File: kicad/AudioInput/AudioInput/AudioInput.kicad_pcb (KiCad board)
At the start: 2 copper layers, 43.2 x 48.3 mm, 52 parts, among them J1 EXPAN2, J2 EXPAN1, K1 G6K-2, Q1 BS250, Q2 2N7000, U1 MCP4651, U2 LM324, U3 CD4052B

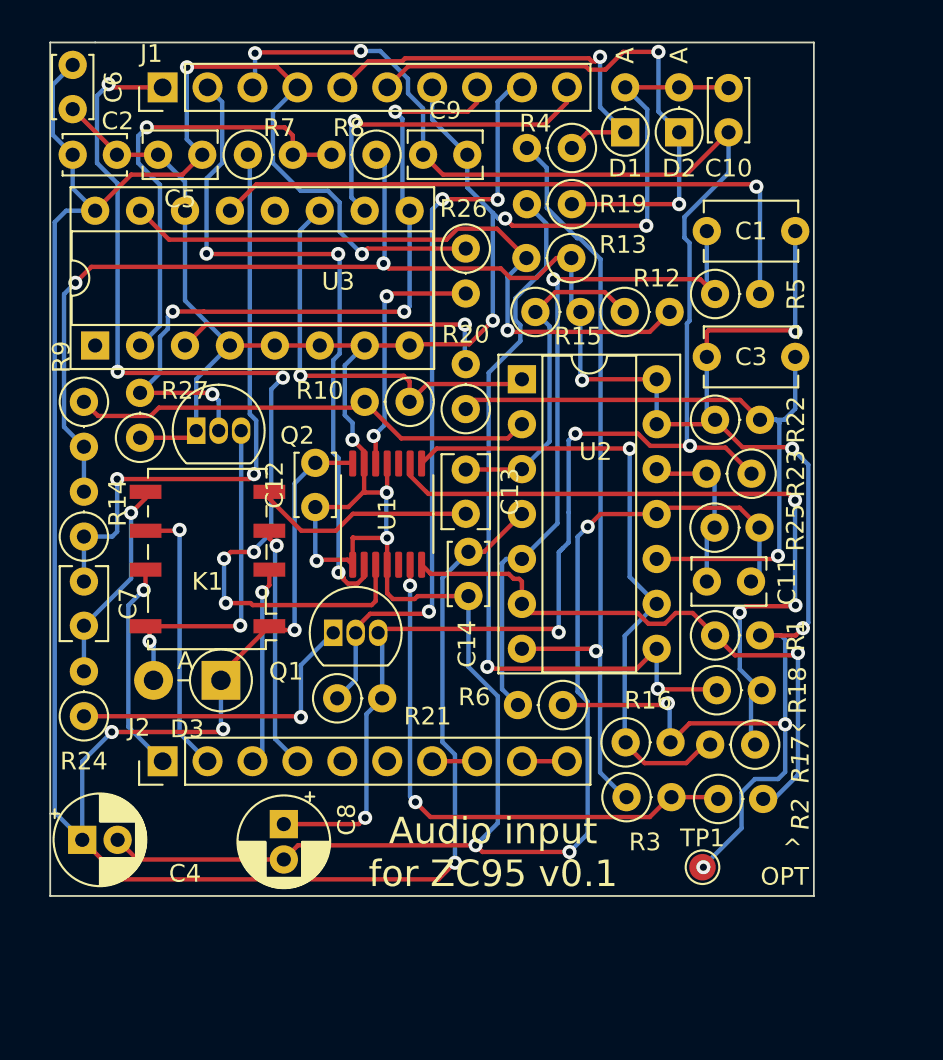
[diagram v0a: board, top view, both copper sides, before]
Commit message: audio input with basic threshold pattern working
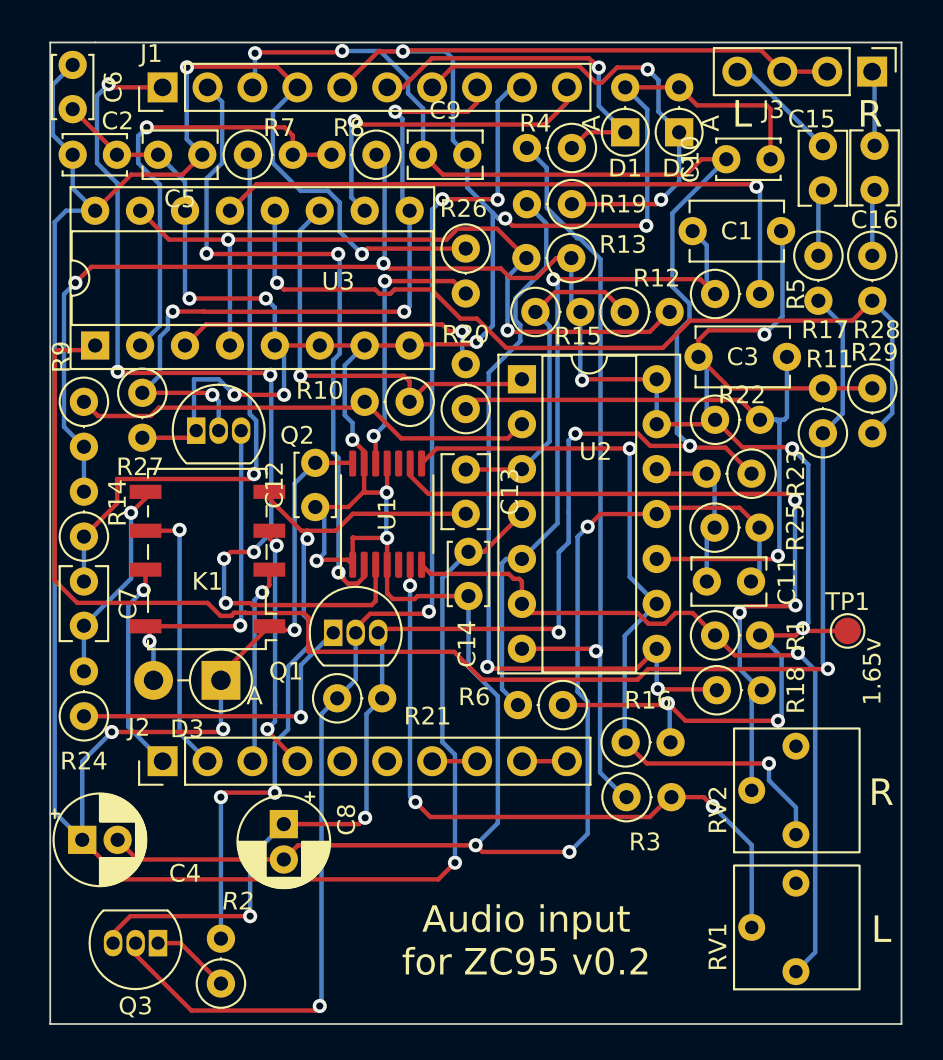
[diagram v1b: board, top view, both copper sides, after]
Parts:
- added C15: 1uF, Capacitor_THT:C_Rect_L4.0mm_W2.5mm_P2.50mm, F.Cu at (173.2, 69.4)
- added C16: 1uF, Capacitor_THT:C_Rect_L4.0mm_W2.5mm_P2.50mm, F.Cu at (176.1, 69.3)
- added J3: INT INPUT, Connector_PinHeader_2.54mm:PinHeader_1x04_P2.54mm_Vertical, F.Cu at (176.0, 65.2)
- added Q3: BS250, Package_TO_SOT_THT:TO-92_Inline, F.Cu at (135.6, 114.4)
- added R11: 150k, Resistor_THT:R_Axial_DIN0207_L6.3mm_D2.5mm_P2.54mm_Vertical, F.Cu at (173.2, 85.6)
- added R28: 100k, Resistor_THT:R_Axial_DIN0207_L6.3mm_D2.5mm_P2.54mm_Vertical, F.Cu at (176.0, 75.6)
- added R29: 150k, Resistor_THT:R_Axial_DIN0207_L6.3mm_D2.5mm_P2.54mm_Vertical, F.Cu at (176.0, 83.1)
- added RV1: 50k, Library:3362P-1-503, F.Cu at (171.7, 113.5)
- added RV2: 50k, Library:3362P-1-503, F.Cu at (171.7, 105.8)
- R1, R16: value 10k -> 4k7
- R17: value 4k7 -> 100k
- R2: value 4k7 -> 2k7
- moved R2 30.0 mm to (139.2, 116.7), turned to 90 degrees
- moved R17 27.9 mm to (173.0, 75.6), turned to -90 degrees
- moved TP1 15.7 mm to (174.6, 96.8)
- moved R27 2.54 mm to (134.7, 83.3), turned to -90 degrees
- moved C10 1.53 mm to (167.8, 70.1), turned to 0 degrees
- moved C1 0.80 mm to (165.9, 74.2)
- moved C3 0.47 mm to (171.2, 81.3)
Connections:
- J1 pad 5: ADC1 -> GND
- J1 pad 6: ADC2 -> ADC1
- J1 pad 7: GND -> ADC2
- R17 pad 1: Net-(R17-Pad1) -> Net-(C15-Pad2)
- R17 pad 2: Net-(R16-Pad1) -> INT_INPUT_L
- R18 pad 2: Net-(R17-Pad1) -> Net-(R18-Pad2)
- R2 pad 1: Net-(R2-Pad1) -> Net-(Q3-Pad1)
- R2 pad 2: Net-(R1-Pad1) -> Net-(C13-Pad2)
- R27 pad 1: GND -> AUDIO_EN
- R27 pad 2: AUDIO_EN -> GND
- R3 pad 2: Net-(R2-Pad1) -> Net-(R3-Pad2)
- U1 pad 6: Net-(R2-Pad1) -> Net-(R3-Pad2)
- U1 pad 9: Net-(R17-Pad1) -> Net-(R18-Pad2)
- U3 pad 1: unconnected-(U3-Pad1) -> INT_INPUT_L
- U3 pad 12: unconnected-(U3-Pad12) -> INT_INPUT_R
- U3 pad 4: GND -> Net-(R12-Pad2)
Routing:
- net INT_INPUT_L: track 0.00 -> 84.9 mm, vias 0 -> 1
- net INT_INPUT_R: track 0.00 -> 49.0 mm, vias 0 -> 1
- net GND: track 190.1 -> 236.1 mm, vias 10 -> 15
- net Net-(R18-Pad2): track 0.00 -> 43.7 mm, vias 0 -> 3
- net Net-(R17-Pad1): track 40.4 -> 0.00 mm, vias 3 -> 0
- net Net-(R3-Pad2): track 0.00 -> 39.1 mm, vias 0 -> 3
- net Net-(R2-Pad1): track 31.3 -> 0.00 mm, vias 2 -> 0
- net MIC_PWR_DIS: track 42.9 -> 73.2 mm, vias 3 -> 4
- net Net-(C13-Pad2): track 12.6 -> 39.6 mm, vias 0 -> 3
- net 3v3: track 102.4 -> 115.7 mm, vias 6 -> 7
- net Net-(R1-Pad1): track 34.3 -> 43.6 mm
- net Net-(R16-Pad1): track 35.7 -> 43.4 mm, vias 1 -> 2
- net Net-(C15-Pad1): track 0.00 -> 6.58 mm
- net Net-(R12-Pad2): track 37.7 -> 43.7 mm, vias 1 -> 2
- net Net-(Q3-Pad1): track 0.00 -> 4.50 mm
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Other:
- board size 43.2 x 48.3 mm -> 48.1 x 55.5 mm
- board text added: "1.65v"
- board text added: "Audio input for ZC95 v0.2"
- board text added: "L"
- board text added: "R"
- board text removed: "Audio input for ZC95 v0.1"
- board text removed: "^"
- board text removed: "^ OPT"

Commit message: mostly documentation of audio input board
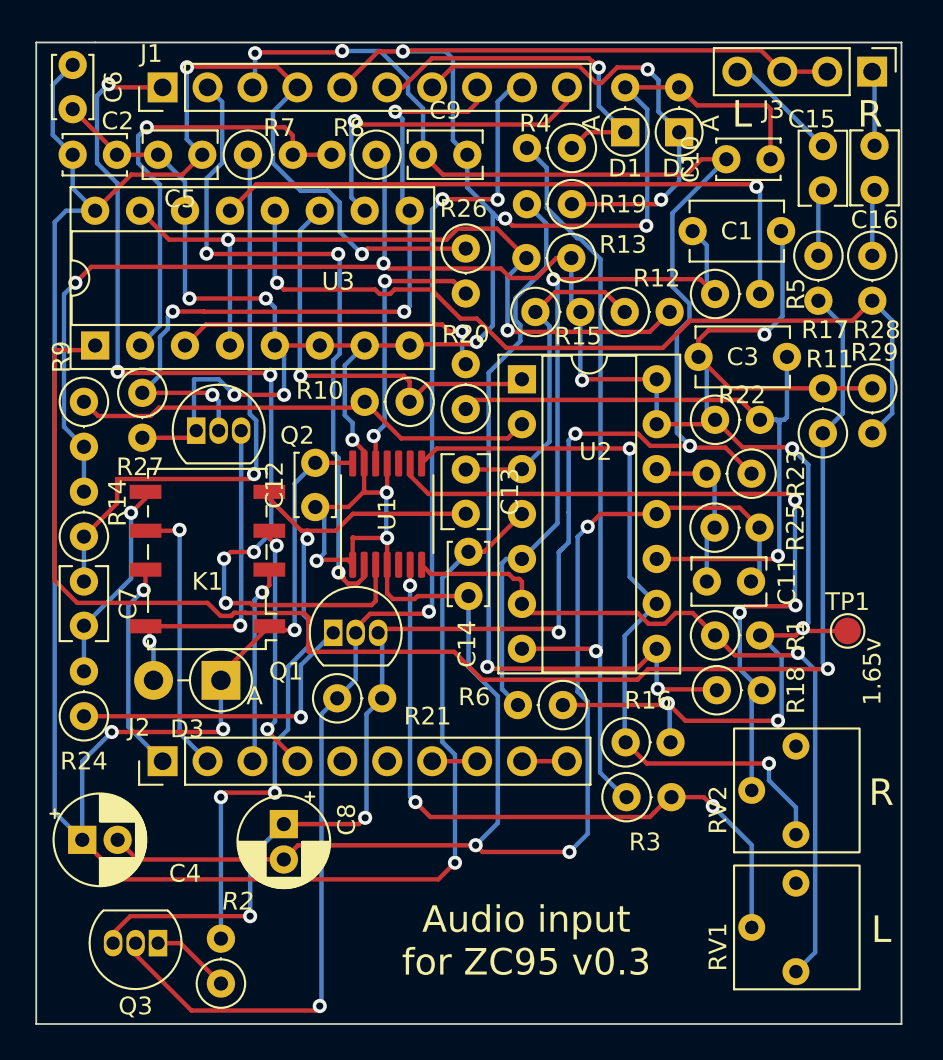
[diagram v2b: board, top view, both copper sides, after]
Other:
- board size 48.1 x 55.5 mm -> 48.9 x 55.5 mm
- board text added: "Audio input for ZC95 v0.3"
- board text removed: "Audio input for ZC95 v0.2"
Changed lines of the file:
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@@
     )
   )
-  (gr_line (start 129.54 63.5) (end 132.08 63.5) (layer "Edge.Cuts") (width 0.1))
+  (gr_line (start 128.75 63.5) (end 132.08 63.5) (layer "Edge.Cuts") (width 0.1))
   (gr_line (start 177.673 63.5) (end 177.673 118.999) (layer "Edge.Cuts") (width 0.1))
-  (gr_line (start 129.54 118.999) (end 129.54 63.5) (layer "Edge.Cuts") (width 0.1))
+  (gr_line (start 128.75 118.999) (end 128.75 63.5) (layer "Edge.Cuts") (width 0.1))
   (gr_line (start 132.08 63.5) (end 177.673 63.5) (layer "Edge.Cuts") (width 0.1))
-  (gr_line (start 177.673 118.999) (end 129.54 118.999) (layer "Edge.Cuts") (width 0.1))
-  (gr_text "Audio input\nfor ZC95 v0.2" (at 156.464 114.3) (layer "F.SilkS")
+  (gr_line (start 177.673 118.999) (end 128.75 118.999) (layer "Edge.Cuts") (width 0.1))
+  (gr_text "Audio input\nfor ZC95 v0.3" (at 156.464 114.3) (layer "F.SilkS")
     (effects (font (size 1.5 1.5) (thickness 0.3)))
   )

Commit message: Audio input board v0.4
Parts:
- removed D1, D2: 3.3v, Diode_THT:D_DO-35_SOD27_P2.54mm_Vertical_AnodeUp
- removed RV1, RV2: 50k, Library:3362P-1-503
- C1: value 3nF -> 3.3nF; footprint Capacitor_THT:C_Disc_D5.1mm_W3.2mm_P5.00mm -> Capacitor_SMD:C_0603_1608Metric_Pad1.08x0.95mm_HandSolder
- C10, C12, C6: footprint Capacitor_THT:C_Disc_D3.4mm_W2.1mm_P2.50mm -> Capacitor_SMD:C_0603_1608Metric_Pad1.08x0.95mm_HandSolder
- C11, C15, C7, C9: footprint Capacitor_THT:C_Rect_L4.0mm_W2.5mm_P2.50mm -> Capacitor_SMD:C_0603_1608Metric_Pad1.08x0.95mm_HandSolder
- C13: value 1uF -> 10uF; footprint Capacitor_THT:C_Rect_L4.0mm_W2.5mm_P2.50mm -> Capacitor_SMD:C_0603_1608Metric_Pad1.08x0.95mm_HandSolder
- C14, C2: value 100nF -> 1uF; footprint Capacitor_THT:C_Disc_D3.4mm_W2.1mm_P2.50mm -> Capacitor_SMD:C_0603_1608Metric_Pad1.08x0.95mm_HandSolder
- C16: value 1uF -> 100nF; footprint Capacitor_THT:C_Rect_L4.0mm_W2.5mm_P2.50mm -> Capacitor_SMD:C_0603_1608Metric_Pad1.08x0.95mm_HandSolder
- C3: value 3nF -> 100nF; footprint Capacitor_THT:C_Disc_D5.1mm_W3.2mm_P5.00mm -> Capacitor_SMD:C_0603_1608Metric_Pad1.08x0.95mm_HandSolder
- C4: footprint Capacitor_THT:CP_Radial_D5.0mm_P2.00mm -> Capacitor_SMD:C_0603_1608Metric_Pad1.08x0.95mm_HandSolder
- C5: value 1uF -> 3.3nF; footprint Capacitor_THT:C_Rect_L4.0mm_W2.5mm_P2.50mm -> Capacitor_SMD:C_0603_1608Metric_Pad1.08x0.95mm_HandSolder
- C8: value 10uF -> 1uF; footprint Capacitor_THT:CP_Radial_D5.0mm_P2.00mm -> Capacitor_SMD:C_0603_1608Metric_Pad1.08x0.95mm_HandSolder
- D3: value 1N4004 -> SM4007PL; footprint Diode_THT:D_DO-41_SOD81_P3.81mm_Vertical_AnodeUp -> Diode_SMD:D_SOD-123F
- Q1: value BS250 -> AO3401A; footprint Package_TO_SOT_THT:TO-92_Inline -> Package_TO_SOT_SMD:SOT-23
- Q2: value 2N7000 -> AO3401A; footprint Package_TO_SOT_THT:TO-92_Inline -> Package_TO_SOT_SMD:SOT-23
- Q3: value BS250 -> AO3400A; footprint Package_TO_SOT_THT:TO-92_Inline -> Package_TO_SOT_SMD:SOT-23
- R1, R11, R12, R15, R17, R21, R23, R25, R26, R27, R28, R29, R3, R4, R7: footprint Resistor_THT:R_Axial_DIN0207_L6.3mm_D2.5mm_P2.54mm_Vertical -> Resistor_SMD:R_0603_1608Metric_Pad0.98x0.95mm_HandSolder
- R10: value 100k -> 4k7; footprint Resistor_THT:R_Axial_DIN0207_L6.3mm_D2.5mm_P2.54mm_Vertical -> Resistor_SMD:R_0603_1608Metric_Pad0.98x0.95mm_HandSolder
- R13, R8: value 150k -> 100k; footprint Resistor_THT:R_Axial_DIN0207_L6.3mm_D2.5mm_P2.54mm_Vertical -> Resistor_SMD:R_0603_1608Metric_Pad0.98x0.95mm_HandSolder
- R14: value 100k -> 150k; footprint Resistor_THT:R_Axial_DIN0207_L6.3mm_D2.5mm_P2.54mm_Vertical -> Resistor_SMD:R_0603_1608Metric_Pad0.98x0.95mm_HandSolder
- R16: value 4k7 -> 100k; footprint Resistor_THT:R_Axial_DIN0207_L6.3mm_D2.5mm_P2.54mm_Vertical -> Resistor_SMD:R_0603_1608Metric_Pad0.98x0.95mm_HandSolder
- R18: value 10k -> 4k7; footprint Resistor_THT:R_Axial_DIN0207_L6.3mm_D2.5mm_P2.54mm_Vertical -> Resistor_SMD:R_0603_1608Metric_Pad0.98x0.95mm_HandSolder
- R19: value 1k -> 10k; footprint Resistor_THT:R_Axial_DIN0207_L6.3mm_D2.5mm_P2.54mm_Vertical -> Resistor_SMD:R_0603_1608Metric_Pad0.98x0.95mm_HandSolder
- R2, R24: value 2k7 -> 2k2; footprint Resistor_THT:R_Axial_DIN0207_L6.3mm_D2.5mm_P2.54mm_Vertical -> Resistor_SMD:R_0603_1608Metric_Pad0.98x0.95mm_HandSolder
- R20: value 10k -> 1k; footprint Resistor_THT:R_Axial_DIN0207_L6.3mm_D2.5mm_P2.54mm_Vertical -> Resistor_SMD:R_0603_1608Metric_Pad0.98x0.95mm_HandSolder
- R22, R6: value 100k -> 10k; footprint Resistor_THT:R_Axial_DIN0207_L6.3mm_D2.5mm_P2.54mm_Vertical -> Resistor_SMD:R_0603_1608Metric_Pad0.98x0.95mm_HandSolder
- R5: value 10k -> 100k; footprint Resistor_THT:R_Axial_DIN0207_L6.3mm_D2.5mm_P2.54mm_Vertical -> Resistor_SMD:R_0603_1608Metric_Pad0.98x0.95mm_HandSolder
- R9: value 10k -> 150k; footprint Resistor_THT:R_Axial_DIN0207_L6.3mm_D2.5mm_P2.54mm_Vertical -> Resistor_SMD:R_0603_1608Metric_Pad0.98x0.95mm_HandSolder
- U2: footprint Package_DIP:DIP-14_W7.62mm_Socket -> Package_SO:SOIC-14_3.9x8.7mm_P1.27mm
- U3: footprint Package_DIP:DIP-16_W7.62mm_Socket -> Package_SO:SOIC-16_3.9x9.9mm_P1.27mm
- moved R28 45.8 mm to (132.5, 89.9), turned to 0 degrees
- moved C4 41.8 mm to (142.6, 68.3), turned to 180 degrees
- moved C2 40.4 mm to (173.7, 69.6), turned to -90 degrees
- moved R18 39.0 mm to (133.6, 80.4), turned to -90 degrees
- moved C11 36.0 mm to (142.6, 69.6), turned to 0 degrees
- moved U3 33.5 mm to (165.6, 80.8), turned to 0 degrees
- moved R16 32.5 mm to (145.0, 75.4), turned to -90 degrees
- moved C8 30.9 mm to (159.0, 81.4), turned to 90 degrees
- moved C10 29.1 mm to (139.2, 75.5), turned to 90 degrees
- moved R9 29.1 mm to (160.1, 79.0), turned to 0 degrees
- moved TP1 29.0 mm to (156.7, 73.9)
- moved C7 28.8 mm to (159.3, 86.5)
- moved Q3 27.6 mm to (132.0, 87.1)
- moved R3 26.9 mm to (145.5, 85.0), turned to -90 degrees
- moved R1 26.7 mm to (145.0, 82.0), turned to 180 degrees
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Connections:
- C10 pad 1: 3v3 -> 5v
- C11 pad 2: Net-(C11-Pad2) -> 5v
- C12 pad 1: GND -> 5v
- C12 pad 2: 5v -> GND
- C13 pad 1: AUDIO_IN_L -> 3v3
- C13 pad 2: Net-(C13-Pad2) -> GND
- C14 pad 2: 5v -> 3v3
- C16 pad 1: Net-(C16-Pad1) -> 3v3
- C16 pad 2: Net-(C16-Pad2) -> GND
- C2 pad 1: GND -> Net-(J3-Pad1)
- C2 pad 2: 5v -> Net-(C2-Pad2)
- C3 pad 1: Net-(C3-Pad1) -> GND
- C3 pad 2: 1.65v -> 5v
- C5 pad 1: 5v -> Net-(U2-Pad10)
- C5 pad 2: GND -> 1.65v
- C8 pad 1: 3v3 -> GND
- C8 pad 2: GND -> Net-(U2-Pad12)
- C9 pad 1: 3v3 -> AUDIO_IN_L
- C9 pad 2: GND -> Net-(K1-Pad4)
- D3 pad 2: Net-(K1-Pad8) -> Net-(D3-Pad2)
- J3 pad 1: Net-(C16-Pad1) -> Net-(J3-Pad1)
- K1 pad 4: Net-(C13-Pad2) -> Net-(K1-Pad4)
- K1 pad 8: Net-(K1-Pad8) -> Net-(D3-Pad2)
- Q1 pad 1: Net-(Q1-Pad1) -> MIC_PWR_DIS
- Q1 pad 2: MIC_PWR_DIS -> 3v3
- Q1 pad 3: 3v3 -> Net-(R24-Pad1)
- Q2 pad 1: GND -> MIC_PWR_DIS
- Q2 pad 2: AUDIO_EN -> 3v3
- Q2 pad 3: Net-(K1-Pad8) -> Net-(R2-Pad1)
- Q3 pad 1: Net-(Q3-Pad1) -> AUDIO_EN
- Q3 pad 2: MIC_PWR_DIS -> GND
- Q3 pad 3: 3v3 -> Net-(D3-Pad2)
- R10 pad 1: MIC_PREAMP_OUT -> Net-(U2-Pad2)
- R10 pad 2: Net-(R10-Pad2) -> 1.65v
- R12 pad 1: AUDIO_IN_L -> Net-(U2-Pad2)
- R12 pad 2: Net-(R12-Pad2) -> MIC_PREAMP_OUT
- R13 pad 1: 1.65v -> AUDIO_IN_L
- R13 pad 2: Net-(R12-Pad2) -> Net-(U3-Pad15)
- R14 pad 1: AUDIO_IN_R -> 1.65v
- R14 pad 2: 1.65v -> Net-(U3-Pad15)
- R15 pad 1: AUDIO_IN_L -> 1.65v
- R15 pad 2: 1.65v -> AUDIO_IN_R
- R16 pad 1: Net-(R16-Pad1) -> 1.65v
- R16 pad 2: 1.65v -> AUDIO_IN_L
- R18 pad 1: Net-(R18-Pad1) -> Net-(U1-Pad8)
- R18 pad 2: Net-(R18-Pad2) -> 1.65v
- R19 pad 1: ADC2 -> Net-(U2-Pad8)
- R19 pad 2: Net-(R18-Pad1) -> Net-(U1-Pad9)
- R2 pad 1: Net-(Q3-Pad1) -> Net-(R2-Pad1)
- R2 pad 2: Net-(C13-Pad2) -> Net-(K1-Pad4)
- R20 pad 1: Net-(C3-Pad1) -> ADC2
- R20 pad 2: AUDIO_R -> Net-(U2-Pad8)
- R22 pad 1: 1.65v -> Net-(U2-Pad10)
- R22 pad 2: Net-(C3-Pad1) -> AUDIO_R
- R23 pad 1: 3v3 -> 1.65v
- R23 pad 2: Net-(C11-Pad2) -> Net-(U2-Pad10)
- R24 pad 1: Net-(Q1-Pad1) -> Net-(R24-Pad1)
- R25 pad 1: Net-(C11-Pad2) -> Net-(U2-Pad12)
- R25 pad 2: GND -> 3v3
- R27 pad 1: AUDIO_EN -> Net-(U2-Pad12)
- R28 pad 1: Net-(C16-Pad2) -> 5v
- R28 pad 2: INT_INPUT_R -> AUDIO_EN
- R5 pad 1: Net-(C1-Pad1) -> Net-(C2-Pad2)
- R5 pad 2: AUDIO_L -> INT_INPUT_R
- R6 pad 1: 1.65v -> Net-(C1-Pad1)
- R6 pad 2: Net-(C1-Pad1) -> AUDIO_L
- R7 pad 2: Net-(R7-Pad2) -> Net-(R9-Pad2)
- R8 pad 2: Net-(R7-Pad2) -> Net-(C1-Pad1)
- R9 pad 1: Net-(R10-Pad2) -> 1.65v
- R9 pad 2: 1.65v -> Net-(R9-Pad2)
- U1 pad 8: Net-(R16-Pad1) -> Net-(U1-Pad8)
- U1 pad 9: Net-(R18-Pad2) -> Net-(U1-Pad9)
- U2 pad 10: Net-(C3-Pad1) -> Net-(U2-Pad10)
- U2 pad 12: Net-(C11-Pad2) -> Net-(U2-Pad12)
- U2 pad 2: Net-(R10-Pad2) -> Net-(U2-Pad2)
- U2 pad 8: Net-(R18-Pad1) -> Net-(U2-Pad8)
- U2 pad 9: Net-(R16-Pad1) -> Net-(U1-Pad8)
- U3 pad 15: Net-(R12-Pad2) -> Net-(U3-Pad15)
- U3 pad 2: Net-(R7-Pad2) -> Net-(R9-Pad2)
- U3 pad 4: Net-(R12-Pad2) -> Net-(U3-Pad15)
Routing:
- net GND: track 236.1 -> 13.7 mm, vias 15 -> 45
- net INT_INPUT_L: track 84.9 -> 11.6 mm, vias 1 -> 0
- net AUDIO_EN: track 42.1 -> 98.3 mm, vias 4 -> 0
- net SDA: track 54.6 -> 4.56 mm, vias 6 -> 0
- net 1.65v: track 132.6 -> 85.9 mm
- net 5v: track 164.8 -> 119.0 mm, vias 6 -> 5
- net Net-(R18-Pad1): track 43.8 -> 0.00 mm, vias 2 -> 0
- net Net-(R18-Pad2): track 43.7 -> 0.00 mm, vias 3 -> 0
- net Net-(R12-Pad2): track 43.7 -> 0.00 mm, vias 2 -> 0
- net Net-(R16-Pad1): track 43.4 -> 0.00 mm, vias 2 -> 0
- net Net-(U3-Pad15): track 0.00 -> 41.7 mm, vias 0 -> 2
- net Net-(C13-Pad2): track 39.6 -> 0.00 mm, vias 3 -> 0
- net Net-(C3-Pad1): track 38.0 -> 0.00 mm, vias 1 -> 0
- net Net-(U2-Pad8): track 0.00 -> 36.9 mm, vias 0 -> 4
- net AUDIO_L: track 36.6 -> 2.51 mm, vias 1 -> 0
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- added copper zone on B.Cu, net GND
- added copper zone on F.Cu, net GND
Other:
- board size 48.9 x 55.5 mm -> 47.9 x 46.6 mm
- board text added: "Audio input for ZC95 v0.4"
- board text removed: "1.65v"
- board text removed: "Audio input for ZC95 v0.3"
- board text removed: "L"
- board text removed: "R"

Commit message: fix drc errors
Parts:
- moved R2 1.52 mm to (150.5, 97.8)
- moved R24 1.40 mm to (147.2, 89.2), turned to 90 degrees
- moved C2 0.89 mm to (173.7, 70.5)
- moved R29 0.89 mm to (170.7, 70.5)
- moved R5 0.89 mm to (172.2, 70.5)
- moved C15 0.81 mm to (166.1, 70.4)
- moved R17 0.81 mm to (164.3, 70.4)
- moved R11 0.79 mm to (162.8, 70.4)
- moved C6 0.76 mm to (142.6, 71.6)
- moved C11 0.51 mm to (142.6, 70.1)
- moved R14 0.48 mm to (141.6, 77.2)
- moved C4 0.25 mm to (142.6, 68.6)
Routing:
- net 5v: track 119.0 -> 116.0 mm
- net Net-(R2-Pad1): track 2.64 -> 4.16 mm
- net Net-(K1-Pad5): track 18.5 -> 19.8 mm
- net INT_INPUT_R: track 21.7 -> 20.7 mm
- net Net-(J3-Pad1): track 1.93 -> 2.83 mm
- net Net-(C15-Pad1): track 1.93 -> 2.75 mm
- net Net-(U2-Pad8): track 36.9 -> 36.1 mm
- net Net-(R24-Pad1): track 2.39 -> 2.97 mm
- net Net-(U3-Pad15): track 41.7 -> 42.3 mm
